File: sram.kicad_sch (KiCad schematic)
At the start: 28 parts, among them J1 Cache_slot, U1 IS61C256AL-12JLI, U10 74F244, U11 74F244, U2 IS61C256AL-12JLI, U3 IS61C256AL-12JLI, U4 IS61C256AL-12JLI, U5 IS61C256AL-12JLI, U6 IS61C256AL-12JLI, U7 IS61C256AL-12JLI, U8 IS61C256AL-12JLI, U9 IS61C3216AL-12TLI

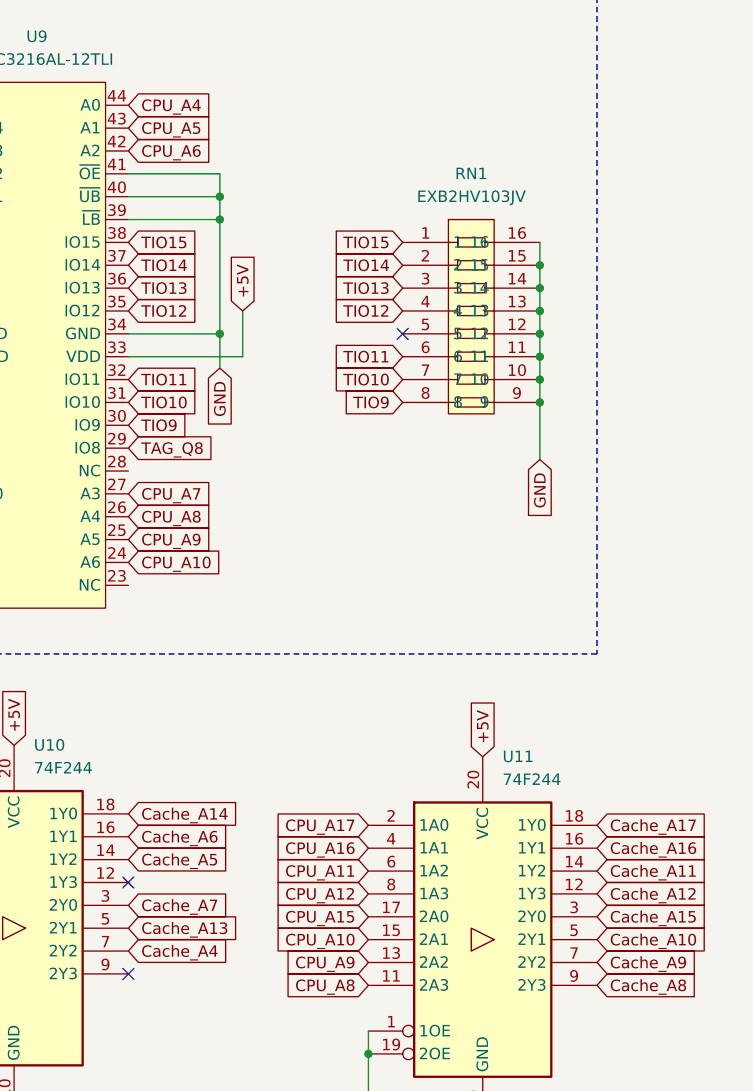
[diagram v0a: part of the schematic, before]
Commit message: change from rasz_pl:  - moving VIAs apart  - change resistor network with single resistor
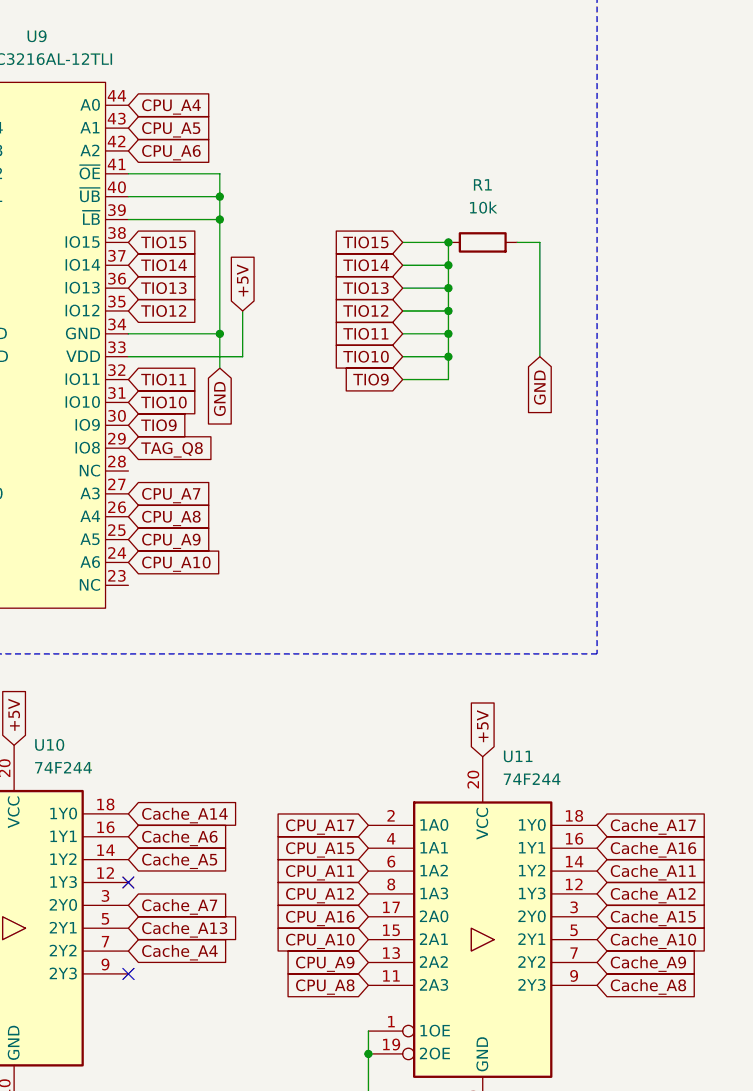
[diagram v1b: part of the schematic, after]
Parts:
- removed RN1: EXB2HV103JV, footprints:RES-ARRAY-SMD_16P-L3.8-W1.6-P0.50-BL, symbol footprints:EXB2HV103JV
- added R1: 10k, Resistor_SMD:R_0805_2012Metric, symbol Device:R
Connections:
- net TIO11 is gone; now on net TIO10: U9.32 (IO11)
- net TIO12 is gone; now on net TIO10: U9.35 (IO12)
- net TIO13 is gone; now on net TIO10: U9.36 (IO13)
- net TIO14 is gone; now on net TIO10: U9.37 (IO14)
- net TIO15 is gone; now on net TIO10: U9.38 (IO15)
- net TIO9 is gone; now on net TIO10: U9.30 (IO9)
- net CPU_A15: now also U11.4 (1A1); no longer U11.17 (2A0)
- net CPU_A16: now also U11.17 (2A0); no longer U11.4 (1A1)
- net GND: now also R1.2
- net TIO10: now also R1.1
- no-connect marks 3 -> 2

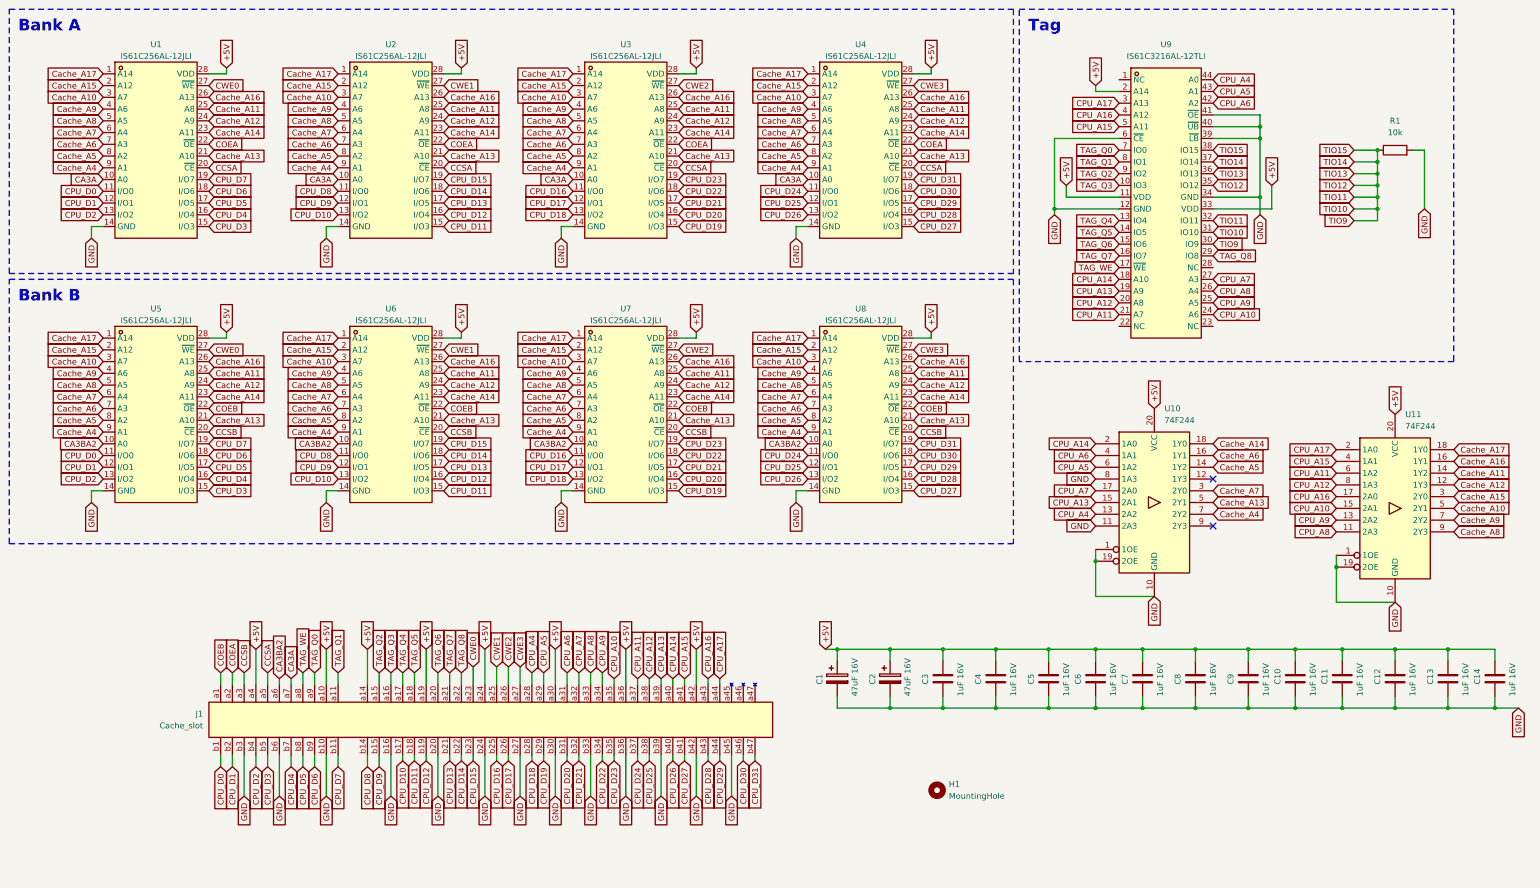
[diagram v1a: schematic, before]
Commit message: updated to 256KB/1MB
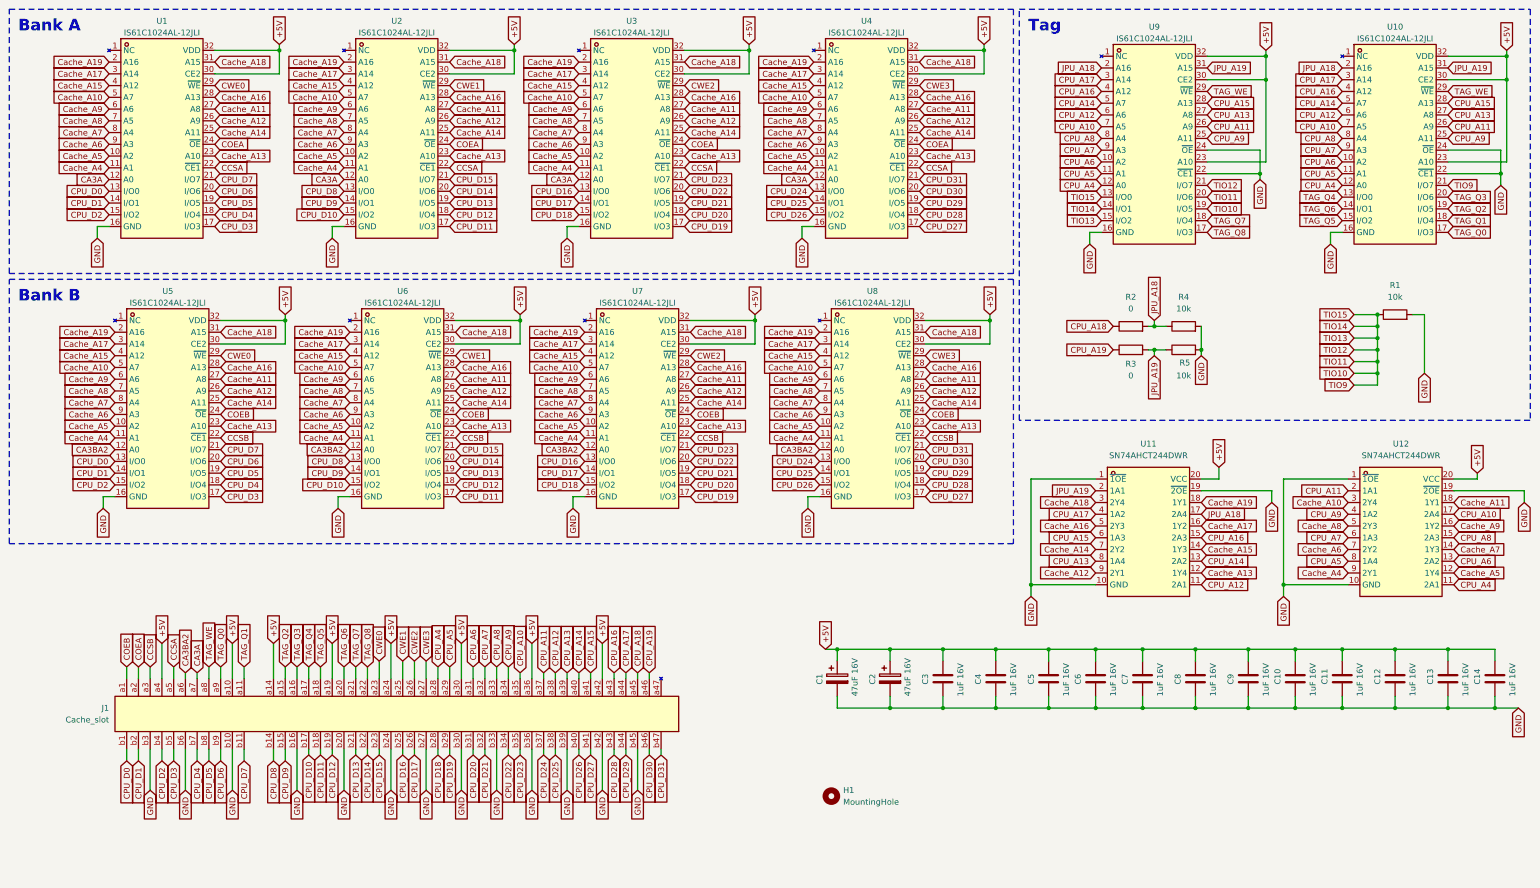
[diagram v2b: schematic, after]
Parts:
- removed U1, U2, U3, U4, U5, U6, U7, U8: IS61C256AL-12JLI, footprints:SOJ-28_L18.1-W7.6-P1.27-LS8.6-BL, symbol footprints:IS61C256AL-12JLI
- removed U10, U11: 74F244, Package_SO:SOIC-20W_7.5x12.8mm_P1.27mm, symbol 74xx:74HCT244
- removed U9: IS61C3216AL-12TLI, footprints:TSOP-44_L18.4-W10.2-P0.80-LS11.8-BL, symbol footprints:IS61C3216AL-12TLI
- added R2, R3: 0, Resistor_SMD:R_0603_1608Metric, symbol Device:R
- added R4, R5: 10k, Resistor_SMD:R_0603_1608Metric, symbol Device:R
- added U1, U10, U2, U3, U4, U5, U6, U7, U8, U9: IS61C1024AL-12JLI, others:SOJ-32_L21.0-W7.6-P1.27-LS8.5-BL, symbol others:IS61C1024AL-12JLI
- added U11, U12: SN74AHCT244DWR, others:SOIC-20_L12.8-W7.5-P1.27-LS10.3-BL, symbol others:SN74AHCT244DWR
- J1: footprint footprints:Cache slot -> others:Cache slot
- R1: footprint Resistor_SMD:R_0805_2012Metric -> Resistor_SMD:R_0603_1608Metric
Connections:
- net +5V: now also U1.30 (CE2), U1.32 (VDD), U10.23 (A10), U10.30 (CE2), U10.32 (VDD), U11.20 (VCC), U12.20 (VCC), U2.30 (CE2), U2.32 (VDD), U3.30 (CE2), U3.32 (VDD), U4.30 (CE2), U4.32 (VDD), U5.30 (CE2), U5.32 (VDD), U6.30 (CE2), U6.32 (VDD), U7.30 (CE2), U7.32 (VDD), U8.30 (CE2), U8.32 (VDD), U9.23 (A10), U9.30 (CE2), U9.32 (VDD)
- net CA3A: now also U1.12 (A0), U2.12 (A0), U3.12 (A0), U4.12 (A0)
- net CA3BA2: now also U5.12 (A0), U6.12 (A0), U7.12 (A0), U8.12 (A0)
- net CCSA: now also U1.22 (~{CE1}), U2.22 (~{CE1}), U3.22 (~{CE1}), U4.22 (~{CE1})
- net CCSB: now also U5.22 (~{CE1}), U6.22 (~{CE1}), U7.22 (~{CE1}), U8.22 (~{CE1})
- net COEA: now also U1.24 (~{OE}), U2.24 (~{OE}), U3.24 (~{OE}), U4.24 (~{OE})
- net COEB: now also U5.24 (~{OE}), U6.24 (~{OE}), U7.24 (~{OE}), U8.24 (~{OE})
- net CPU_A10: now also U10.7 (A5), U12.17 (2A4), U9.7 (A5)
- net CPU_A11: now also U10.26 (A9), U12.2 (1A1), U9.26 (A9)
- net CPU_A12: now also U10.6 (A6), U11.11 (2A1), U9.6 (A6)
- net CPU_A13: now also U10.27 (A8), U11.8 (1A4), U9.27 (A8)
- net CPU_A14: now also U10.5 (A7), U11.13 (2A2), U9.5 (A7)
- net CPU_A15: now also U10.28 (A13), U11.6 (1A3), U9.28 (A13)
- net CPU_A16: now also U10.4 (A12), U11.15 (2A3), U9.4 (A12)
- net CPU_A17: now also U10.3 (A14), U11.4 (1A2), U9.3 (A14)
- net CPU_A4: now also U10.12 (A0), U12.11 (2A1), U9.12 (A0)
- net CPU_A5: now also U10.11 (A1), U12.8 (1A4), U9.11 (A1)
- net CPU_A6: now also U10.10 (A2), U12.13 (2A2), U9.10 (A2)
- net CPU_A7: now also U10.9 (A3), U12.6 (1A3), U9.9 (A3)
- net CPU_A8: now also U10.8 (A4), U12.15 (2A3), U9.8 (A4)
- net CPU_A9: now also U10.25 (A11), U12.4 (1A2), U9.25 (A11)
- net CPU_D0: now also U1.13 (I/O0), U5.13 (I/O0)
- net CPU_D1: now also U1.14 (I/O1), U5.14 (I/O1)
- net CPU_D10: now also U2.15 (I/O2), U6.15 (I/O2)
- net CPU_D11: now also U2.17 (I/O3), U6.17 (I/O3)
- net CPU_D12: now also U2.18 (I/O4), U6.18 (I/O4)
- net CPU_D13: now also U2.19 (I/O5), U6.19 (I/O5)
- net CPU_D14: now also U2.20 (I/O6), U6.20 (I/O6)
- net CPU_D15: now also U2.21 (I/O7), U6.21 (I/O7)
- net CPU_D16: now also U3.13 (I/O0), U7.13 (I/O0)
- net CPU_D17: now also U3.14 (I/O1), U7.14 (I/O1)
- net CPU_D18: now also U3.15 (I/O2), U7.15 (I/O2)
- net CPU_D19: now also U3.17 (I/O3), U7.17 (I/O3)
- net CPU_D2: now also U1.15 (I/O2), U5.15 (I/O2)
- net CPU_D20: now also U3.18 (I/O4), U7.18 (I/O4)
- net CPU_D21: now also U3.19 (I/O5), U7.19 (I/O5)
- net CPU_D22: now also U3.20 (I/O6), U7.20 (I/O6)
- net CPU_D23: now also U3.21 (I/O7), U7.21 (I/O7)
- net CPU_D24: now also U4.13 (I/O0), U8.13 (I/O0)
- net CPU_D25: now also U4.14 (I/O1), U8.14 (I/O1)
- net CPU_D26: now also U4.15 (I/O2), U8.15 (I/O2)
- net CPU_D27: now also U4.17 (I/O3), U8.17 (I/O3)
- net CPU_D28: now also U4.18 (I/O4), U8.18 (I/O4)
- net CPU_D29: now also U4.19 (I/O5), U8.19 (I/O5)
- net CPU_D3: now also U1.17 (I/O3), U5.17 (I/O3)
- net CPU_D30: now also U4.20 (I/O6), U8.20 (I/O6)
- net CPU_D31: now also U4.21 (I/O7), U8.21 (I/O7)
- net CPU_D4: now also U1.18 (I/O4), U5.18 (I/O4)
- net CPU_D5: now also U1.19 (I/O5), U5.19 (I/O5)
- net CPU_D6: now also U1.20 (I/O6), U5.20 (I/O6)
- net CPU_D7: now also U1.21 (I/O7), U5.21 (I/O7)
- net CPU_D8: now also U2.13 (I/O0), U6.13 (I/O0)
- net CPU_D9: now also U2.14 (I/O1), U6.14 (I/O1)
- net CWE0: now also U1.29 (~{WE}), U5.29 (~{WE})
- net CWE1: now also U2.29 (~{WE}), U6.29 (~{WE})
- net CWE2: now also U3.29 (~{WE}), U7.29 (~{WE})
- net CWE3: now also U4.29 (~{WE}), U8.29 (~{WE})
- net Cache_A10: now also U1.5 (A7), U12.3 (2Y4), U2.5 (A7), U3.5 (A7), U4.5 (A7), U5.5 (A7), U6.5 (A7), U7.5 (A7), U8.5 (A7)
- net Cache_A11: now also U1.27 (A8), U12.18 (1Y1), U2.27 (A8), U3.27 (A8), U4.27 (A8), U5.27 (A8), U6.27 (A8), U7.27 (A8), U8.27 (A8)
- net Cache_A12: now also U1.26 (A9), U11.9 (2Y1), U2.26 (A9), U3.26 (A9), U4.26 (A9), U5.26 (A9), U6.26 (A9), U7.26 (A9), U8.26 (A9)
- net Cache_A13: now also U1.23 (A10), U11.12 (1Y4), U2.23 (A10), U3.23 (A10), U4.23 (A10), U5.23 (A10), U6.23 (A10), U7.23 (A10), U8.23 (A10)
- net Cache_A14: now also U1.25 (A11), U11.7 (2Y2), U2.25 (A11), U3.25 (A11), U4.25 (A11), U5.25 (A11), U6.25 (A11), U7.25 (A11), U8.25 (A11)
- net Cache_A15: now also U1.4 (A12), U11.14 (1Y3), U2.4 (A12), U3.4 (A12), U4.4 (A12), U5.4 (A12), U6.4 (A12), U7.4 (A12), U8.4 (A12)
- net Cache_A16: now also U1.28 (A13), U11.5 (2Y3), U2.28 (A13), U3.28 (A13), U4.28 (A13), U5.28 (A13), U6.28 (A13), U7.28 (A13), U8.28 (A13)
- net Cache_A17: now also U1.3 (A14), U11.16 (1Y2), U2.3 (A14), U3.3 (A14), U4.3 (A14), U5.3 (A14), U6.3 (A14), U7.3 (A14), U8.3 (A14)
- net Cache_A4: now also U1.11 (A1), U12.9 (2Y1), U2.11 (A1), U3.11 (A1), U4.11 (A1), U5.11 (A1), U6.11 (A1), U7.11 (A1), U8.11 (A1)
- net Cache_A5: now also U1.10 (A2), U12.12 (1Y4), U2.10 (A2), U3.10 (A2), U4.10 (A2), U5.10 (A2), U6.10 (A2), U7.10 (A2), U8.10 (A2)
- net Cache_A6: now also U1.9 (A3), U12.7 (2Y2), U2.9 (A3), U3.9 (A3), U4.9 (A3), U5.9 (A3), U6.9 (A3), U7.9 (A3), U8.9 (A3)
- net Cache_A7: now also U1.8 (A4), U12.14 (1Y3), U2.8 (A4), U3.8 (A4), U4.8 (A4), U5.8 (A4), U6.8 (A4), U7.8 (A4), U8.8 (A4)
- net Cache_A8: now also U1.7 (A5), U12.5 (2Y3), U2.7 (A5), U3.7 (A5), U4.7 (A5), U5.7 (A5), U6.7 (A5), U7.7 (A5), U8.7 (A5)
- net Cache_A9: now also U1.6 (A6), U12.16 (1Y2), U2.6 (A6), U3.6 (A6), U4.6 (A6), U5.6 (A6), U6.6 (A6), U7.6 (A6), U8.6 (A6)
- net GND: now also R4.2, R5.2, U1.16 (GND), U10.16 (GND), U10.22 (~{CE1}), U10.24 (~{OE}), U11.1 (~{1OE}), U11.10 (GND), U11.19 (~{2OE}), U12.1 (~{1OE}), U12.10 (GND), U12.19 (~{2OE}), U2.16 (GND), U3.16 (GND), U4.16 (GND), U5.16 (GND), U6.16 (GND), U7.16 (GND), U8.16 (GND), U9.16 (GND), U9.22 (~{CE1}), U9.24 (~{OE})
- net TAG_Q0: now also U10.17 (I/O3)
- net TAG_Q1: now also U10.18 (I/O4)
- net TAG_Q2: now also U10.19 (I/O5)
- net TAG_Q3: now also U10.20 (I/O6)
- net TAG_Q4: now also U10.13 (I/O0)
- net TAG_Q5: now also U10.15 (I/O2)
- net TAG_Q6: now also U10.14 (I/O1)
- net TAG_Q7: now also U9.18 (I/O4)
- net TAG_Q8: now also U9.17 (I/O3)
- net TAG_WE: now also U10.29 (~{WE}), U9.29 (~{WE})
- net TIO10: now also U10.21 (I/O7), U9.13 (I/O0), U9.14 (I/O1), U9.15 (I/O2), U9.19 (I/O5), U9.20 (I/O6), U9.21 (I/O7)
- net CPU_A18: now reaches J1.a45
- net CPU_A18: now also R2.1
- net CPU_A19: now reaches J1.a46
- net CPU_A19: now also R3.1
- new net Cache_A18: U1.31 (A15), U11.3 (2Y4), U2.31 (A15), U3.31 (A15), U4.31 (A15), U5.31 (A15), U6.31 (A15), U7.31 (A15), U8.31 (A15)
- new net Cache_A19: U1.2 (A16), U11.18 (1Y1), U2.2 (A16), U3.2 (A16), U4.2 (A16), U5.2 (A16), U6.2 (A16), U7.2 (A16), U8.2 (A16)
- new net JPU_A18: R2.2, R4.1, U10.2 (A16), U11.17 (2A4), U9.2 (A16)
- new net JPU_A19: R3.2, R5.1, U10.31 (A15), U11.2 (1A1), U9.31 (A15)
- no-connect marks 2 -> 0
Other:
- title: 256Kb Cache slot for Compaq (197005-001 replacement) -> 1MB Cache slot for Compaq (197005-001 replacement)
- moved on the sheet: H1, R1

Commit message: added switch to set memory size
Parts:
- removed R4, R5: 10k, Resistor_SMD:R_0603_1608Metric, symbol Device:R
- added FID1, FID2, FID3, FID4: Fiducial, Fiducial:Fiducial_0.5mm_Mask1mm, symbol Mechanical:Fiducial
- added SW1: DSIC04TSGET, others:SW-SMD_8P-L11.1-W6.2-P2.54-LS9.8, symbol others:DSIC04TSGET
- R2, R3: value 0 -> 10k
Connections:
- net CPU_A18: now also SW1.2 (A2); no longer R2.1
- net CPU_A19: now also SW1.3 (A3); no longer R3.1
- net GND: now also R2.1, R3.1
- net JPU_A18: now also SW1.7 (B2), SW1.8 (B1); no longer R2.2
- net JPU_A19: now also SW1.5 (B4), SW1.6 (B3); no longer R3.2
- new net: R3.2, SW1.1 (A1)
- new net: R2.2, SW1.4 (A4)
